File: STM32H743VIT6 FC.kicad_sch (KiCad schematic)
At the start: 104 parts, among them SW2 Y78B22310FP, U1 TPS54302DDCR, U2 USBLC6-2SC6, U3 TPS54302DDCR

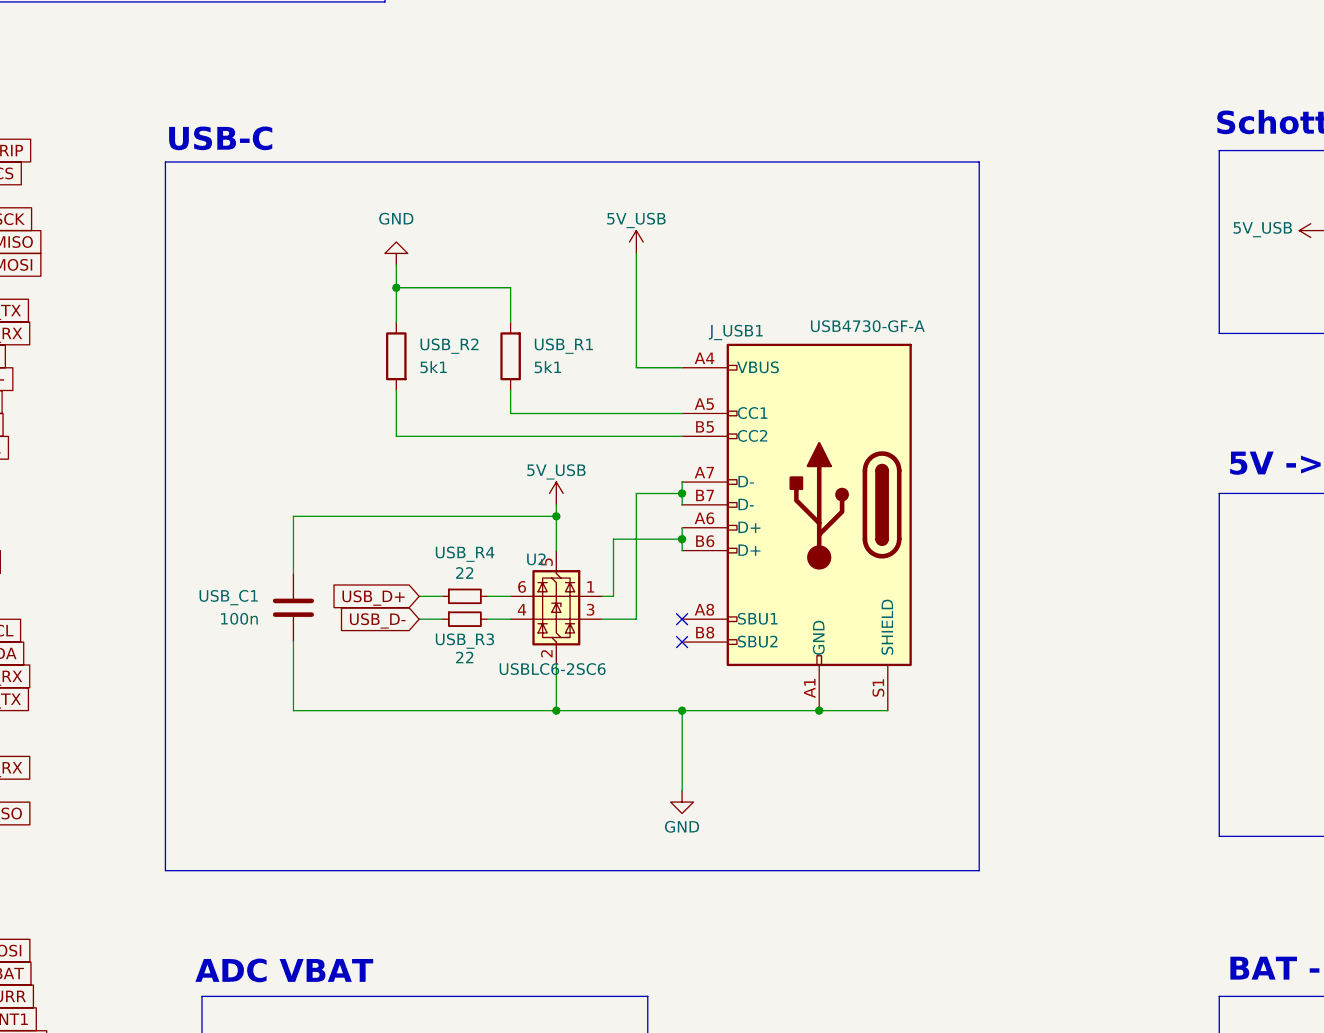
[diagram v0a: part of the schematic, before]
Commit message: Fixed usb footprint.
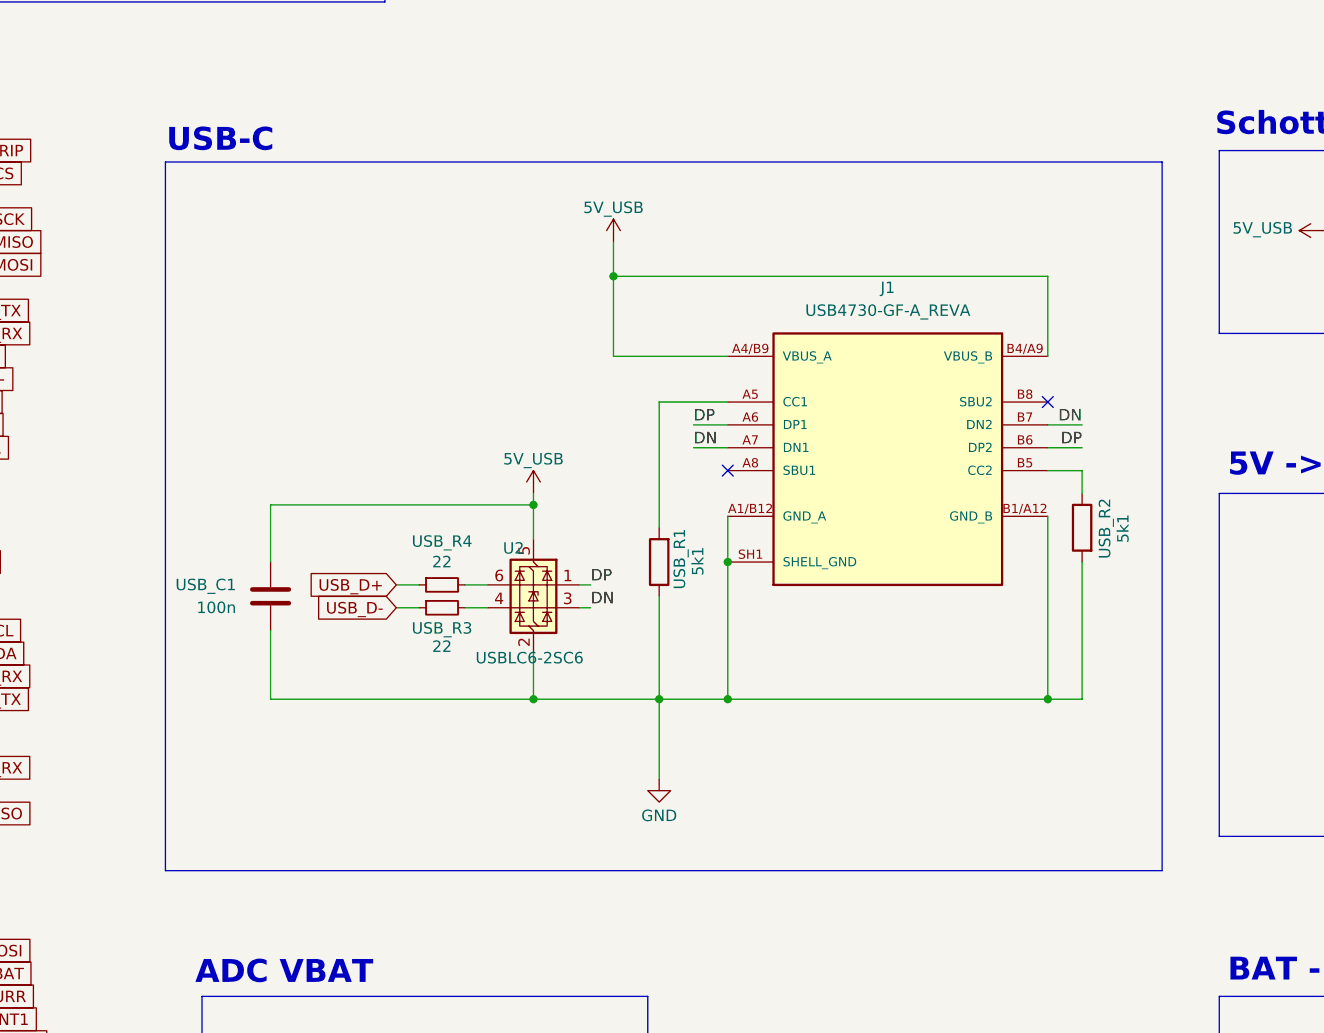
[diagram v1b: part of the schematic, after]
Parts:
- removed J_USB1: USB4730-GF-A, All:GCT_USB4730-GF-A_REVA, symbol Connector:USB_C_Receptacle_USB2.0_16P
- added J1: USB4730-GF-A_REVA, All:GCT_USB4730-GF-A_REVA, symbol USB:USB4730-GF-A_REVA
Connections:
- net 5V_USB: now also J1.A4/B9 (VBUS_A), J1.B4/A9 (VBUS_B)
- net GND: now also USB_R1.1, USB_R2.2, J1.A1/B12 (GND_A), J1.B1/A12 (GND_B), J1.SH1 (SHELL_GND), J1.SH2 (SHELL_GND), J1.SH3 (SHELL_GND), J1.SH4 (SHELL_GND); no longer USB_R1.2, USB_R2.1
- net DP: now reaches U2.1 (I/O1)
- net DP: now also J1.A6 (DP1), J1.B6 (DP2)
- net DN: now reaches U2.3 (I/O2)
- net DN: now also J1.A7 (DN1), J1.B7 (DN2)
- new net: J1.A5 (CC1), USB_R1.2
- new net: J1.B5 (CC2), USB_R2.1
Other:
- moved on the sheet: U2, USB_C1, USB_R1, USB_R2, USB_R3, USB_R4

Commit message: minor
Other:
- moved on the sheet: USB_R2
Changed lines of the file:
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@@
 	)
 	(junction
-		(at 375.92 78.74)
-		(diameter 0)
-		(color 0 0 0 0)
-	)
-	(junction
 		(at 396.24 267.97)
 		(diameter 0)
@@
 	)
 	(junction
+		(at 406.4 76.2)
+		(diameter 0)
+		(color 0 0 0 0)
+	)
+	(junction
 		(at 284.48 35.56)
 		(diameter 0)
@@
 	(wire
 		(pts
-			(xy 427.99 100.33) (xy 427.99 102.87)
+			(xy 429.26 100.33) (xy 429.26 106.68)
 		)
 		(stroke
@@
 	(wire
 		(pts
-			(xy 424.18 100.33) (xy 427.99 100.33)
+			(xy 424.18 100.33) (xy 429.26 100.33)
 		)
 		(stroke
@@
 	(wire
 		(pts
-			(xy 375.92 74.93) (xy 375.92 78.74)
+			(xy 406.4 73.66) (xy 406.4 76.2)
 		)
 		(stroke
@@
 	(wire
 		(pts
-			(xy 375.92 87.63) (xy 388.62 87.63)
+			(xy 387.35 87.63) (xy 388.62 87.63)
 		)
 		(stroke
@@
 	(wire
 		(pts
-			(xy 427.99 110.49) (xy 427.99 125.73)
+			(xy 429.26 114.3) (xy 429.26 125.73)
 		)
 		(stroke
@@
 	(wire
 		(pts
-			(xy 427.99 125.73) (xy 424.18 125.73)
+			(xy 429.26 125.73) (xy 424.18 125.73)
 		)
 		(stroke
@@
 	(wire
 		(pts
+			(xy 425.45 87.63) (xy 424.18 87.63)
+		)
+		(stroke
+			(width 0)
+			(type default)
+		)
+	)
+	(wire
+		(pts
 			(xy 90.17 165.1) (xy 77.47 165.1)
 		)
@@
 	(wire
 		(pts
-			(xy 424.18 78.74) (xy 424.18 87.63)
+			(xy 425.45 76.2) (xy 425.45 87.63)
 		)
 		(stroke
@@
 	(wire
 		(pts
-			(xy 375.92 78.74) (xy 375.92 87.63)
+			(xy 387.35 76.2) (xy 387.35 87.63)
 		)
 		(stroke
@@
 	(wire
 		(pts
+			(xy 406.4 76.2) (xy 425.45 76.2)
+		)
+		(stroke
+			(width 0)
+			(type default)
+		)
+	)
+	(wire
+		(pts
 			(xy 381 106.68) (xy 381 92.71)
 		)
@@
 	(wire
 		(pts
-			(xy 375.92 78.74) (xy 424.18 78.74)
+			(xy 387.35 76.2) (xy 406.4 76.2)
 		)
 		(stroke
@@
 	(symbol
 		(lib_id "Device:R")
-		(at 427.99 106.68 0)
+		(at 429.26 110.49 0)
 		(mirror y)
 		(unit 1)
@@
 		(dnp no)
 		(property "Reference" "USB_R2"
-			(at 430.53 103.378 90)
+			(at 431.8 107.188 90)
 			(effects
 				(font
@@
 		)
 		(property "Value" "5k1"
-			(at 432.562 105.156 90)
+			(at 433.832 108.966 90)
 			(effects
 				(font
@@
 		)
 		(property "Footprint" "Resistor_SMD:R_0603_1608Metric_Pad0.98x0.95mm_HandSolder"
-			(at 429.768 106.68 90)
+			(at 431.038 110.49 90)
 			(effects
 				(font
@@
 		)
 		(property "Datasheet" "~"
-			(at 427.99 106.68 0)
+			(at 429.26 110.49 0)
 			(effects
 				(font
@@
 		)
 		(property "Description" "Resistor"
-			(at 427.99 106.68 0)
+			(at 429.26 110.49 0)
 			(effects
 				(font
@@
 		)
 		(property "LCSC Part" ""
-			(at 427.99 106.68 0)
+			(at 429.26 110.49 0)
 			(effects
 				(font
@@
 	(symbol
 		(lib_id "power:+3.3V")
-		(at 375.92 74.93 0)
+		(at 406.4 73.66 0)
 		(unit 1)
 		(exclude_from_sim no)
@@
 		(dnp no)
 		(property "Reference" "#PWR037"
-			(at 375.92 78.74 0)
+			(at 406.4 77.47 0)
 			(effects
 				(font
@@
 		)
 		(property "Value" "5V_USB"
-			(at 375.92 71.12 0)
+			(at 406.4 69.85 0)
 			(effects
 				(font
@@
 		)
 		(property "Footprint" ""
-			(at 375.92 74.93 0)
+			(at 406.4 73.66 0)
 			(effects
 				(font
@@
 		)
 		(property "Datasheet" ""
-			(at 375.92 74.93 0)
+			(at 406.4 73.66 0)
 			(effects
 				(font
@@
 		)
 		(property "Description" "Power symbol creates a global label with name \"+3.3V\""
-			(at 375.92 74.93 0)
+			(at 406.4 73.66 0)
 			(effects
 				(font

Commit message: boom
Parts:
- removed AVTX_J1: SM06B-SRSS-TB, All:SM06BSRSSTBLFSN, symbol Connector:Conn_01x06_Pin
- removed BARO_C1, BARO_C2: 100n, Capacitor_SMD:C_0603_1608Metric_Pad1.08x0.95mm_HandSolder, symbol Device:C_Small
- removed BARO_R1, BARO_R2, BARO_R3: 10k, Resistor_SMD:R_0603_1608Metric_Pad0.98x0.95mm_HandSolder, symbol Device:R
- removed DEBUG_J1, RX_J1, UART2_J1: SM04B-SRSS-TB, All:CONN_SM04B-SRSS-TB_JST, symbol Connector:Conn_01x04_Pin
- removed H1, H2, H3, H4: MountingHole, MountingHole:MountingHole_4.3mm_M4, symbol Mechanical:MountingHole
- removed U_BARO1: DPS310, All:XDCR_DPS310, symbol DPS310:DPS310
- MCU_D1, MCU_D2, MCU_D3, USB_D1: footprint LED_SMD:LED_0603_1608Metric -> LED_SMD:LED_0603_1608Metric_Pad1.05x0.95mm_HandSolder
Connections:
- no-connect marks 48 -> 47
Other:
- note removed: "Barometer"
- note removed: "Mounting Holes"

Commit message: Changed inductor and added net classes.
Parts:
- 9V_L1: footprint Inductor_SMD:L_0603_1608Metric_Pad1.05x0.95mm_HandSolder -> Inductor_SMD:L_Wuerth_MAPI-5030
- MCU_R1: value 10K -> 10k

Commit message: Added second inductor.
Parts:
- 5V_L1: footprint Inductor_SMD:L_0603_1608Metric_Pad1.05x0.95mm_HandSolder -> Inductor_SMD:L_Wuerth_MAPI-5030
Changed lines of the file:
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@@
 			)
 		)
-		(property "Footprint" "Inductor_SMD:L_0603_1608Metric_Pad1.05x0.95mm_HandSolder"
+		(property "Footprint" "Inductor_SMD:L_Wuerth_MAPI-5030"
 			(at 524.51 177.8 0)
 			(effects

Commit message: layout
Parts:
- removed MCU_C7: 100n, Capacitor_SMD:C_0603_1608Metric_Pad1.08x0.95mm_HandSolder, symbol Device:C
- removed MCU_C8: 1u, Capacitor_SMD:C_0603_1608Metric_Pad1.08x0.95mm_HandSolder, symbol Device:C
- J1: value USB4730-GF-A_REVA -> USB4730-GF-A
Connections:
- net DN: now also U2.1 (I/O1); no longer J1.A7 (DN1), U2.3 (I/O2)
- net DP: now also U2.3 (I/O2); no longer J1.A6 (DP1), U2.1 (I/O1)
- net USB_D+: now also USB_R3.1; no longer USB_R4.1
- net USB_D-: now also USB_R4.1; no longer USB_R3.1
- no-connect marks 47 -> 49
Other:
- note removed: "VREF"

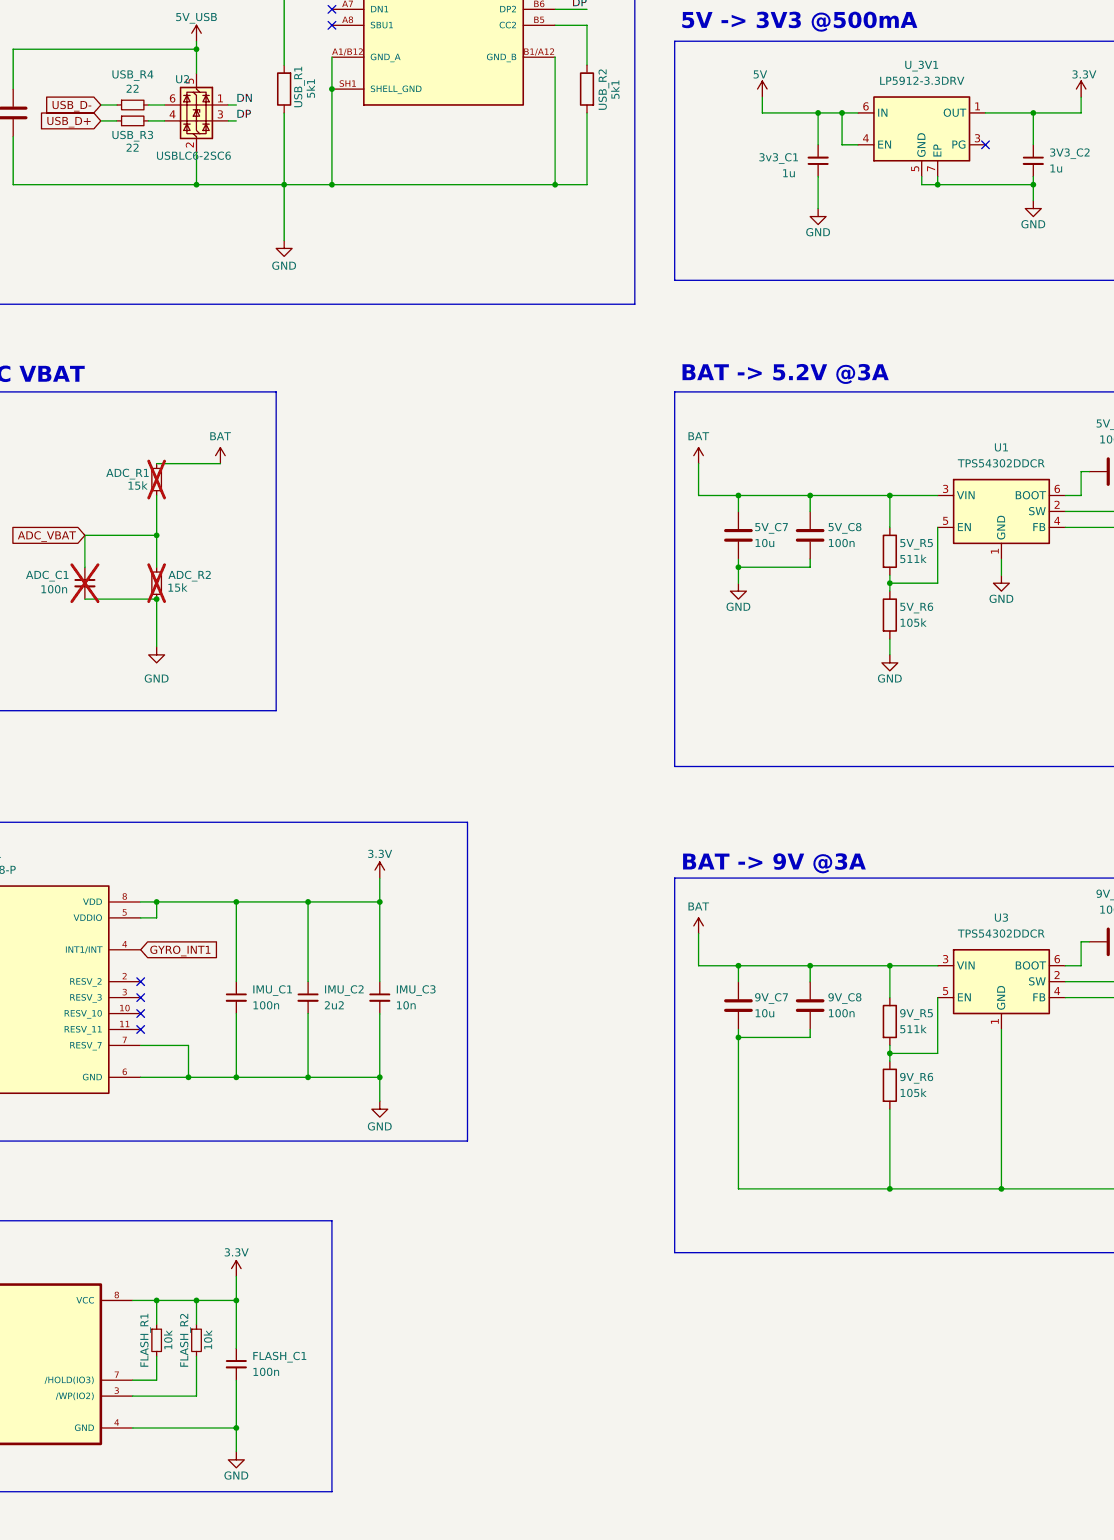
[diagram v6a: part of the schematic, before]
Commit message: Removed EN resistors from bucks.
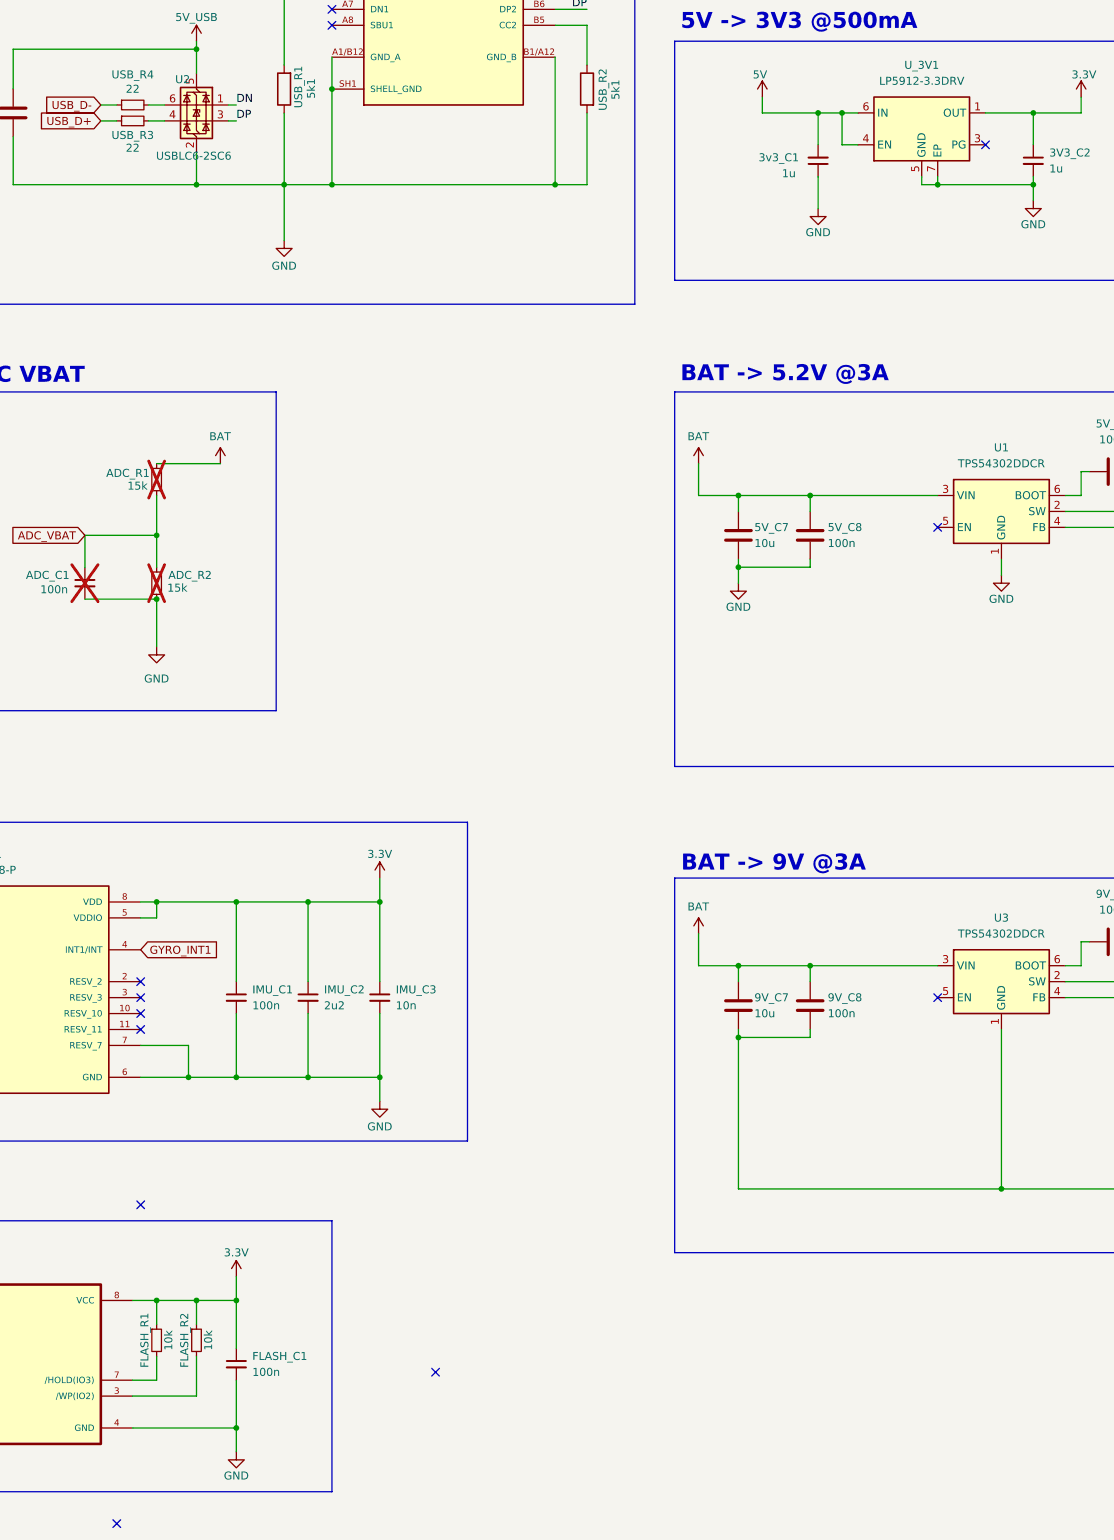
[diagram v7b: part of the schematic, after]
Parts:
- removed 5V_R5, 9V_R5: 511k, Resistor_SMD:R_0603_1608Metric_Pad0.98x0.95mm_HandSolder, symbol Device:R
- removed 5V_R6, 9V_R6: 105k, Resistor_SMD:R_0603_1608Metric_Pad0.98x0.95mm_HandSolder, symbol Device:R
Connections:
- no-connect marks 49 -> 54

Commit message: more
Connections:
- net 3.3V: now also AVTX_J2.1 (Pin_1)
- net 9V_REG: no longer AVTX_J2.1 (Pin_1)
- no-connect marks 54 -> 51
